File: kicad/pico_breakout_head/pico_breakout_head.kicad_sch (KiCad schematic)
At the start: 16 parts, among them J1 Conn_01x03, J2 JST PH 5-pin male thru vertic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, J3 Conn_01x03, J34 Conn_01x03, J4 Conn_01x03, J5 XH2.54

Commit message: PCB updated to product
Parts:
- removed J2: JST PH 5-pin male thru vertical, Connector_JST:JST_PH_B5B-PH-K_1x05_P2.00mm_Vertical, symbol Connector_Generic:Conn_01x05
- added J2: Conn_01x06, symbol Connector_Generic:Conn_01x06
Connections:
- net +5V: now also U2.39 (VSYS), J2.1 (Pin_1); no longer U2.40 (VBUS)
- net GND: now also J2.6 (Pin_6)
- net SCL_ESP32: now also J2.3 (Pin_3)
- net SDA_ESP32: now also J2.4 (Pin_4)
- new net INT_ESP32: J2.5 (Pin_5)
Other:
- moved on the sheet: U2

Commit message: Pico head WiP
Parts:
- removed J2: Conn_01x06, symbol Connector_Generic:Conn_01x06
- removed J3, J34, J4: Conn_01x03, symbol Connector_Generic:Conn_01x03
- added H1, H2, H3, H4: MountingHole, MountingHole:MountingHole_3.2mm_M3, symbol Mechanical:MountingHole
- added J1: JST B6B-PH-K-S, Connector_JST:JST_PH_B6B-PH-K_1x06_P2.00mm_Vertical, symbol Connector_Generic:Conn_01x06
- added J2, J3: HDR F 2.54MM 20-pin VERT, symbol Connector_Generic:Conn_01x20
- added J4: HDR M 2.54MM 9-pin VERT, symbol Connector_Generic:Conn_01x09
- renumbered J1 to J6
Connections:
- net +3.3V: now also J3.5 (Pin_5)
- net +5V: now also J1.1 (Pin_1), J3.2 (Pin_2), J4.2 (Pin_2), J4.4 (Pin_4), J4.7 (Pin_7)
- net GND: now also J1.6 (Pin_6), J2.13 (Pin_13), J2.18 (Pin_18), J2.8 (Pin_8), J3.13 (Pin_13), J3.18 (Pin_18), J3.3 (Pin_3), J3.8 (Pin_8), J4.1 (Pin_1), J4.5 (Pin_5), J4.8 (Pin_8)
- net SERVO_LEFT: now also U2.5 (I2C1_SCL/SPI0_TX/GP3), J2.5 (Pin_5), J4.3 (Pin_3)
- net SERVO_RIGHT: now also U2.6 (UART1_TX/I2C0_SDA/SPI0_RX/GP4), J2.6 (Pin_6), J4.6 (Pin_6)
- net I2C_SDA_MASTER: now reaches U2.1 (UART0_TX/I2C0_SDA/SPI0_RX/GP0)
- net I2C_SDA_MASTER: now also J1.4 (Pin_4), J2.1 (Pin_1)
- net at U2.10 (I2C1_SCL/SPI0_TX/GP7): now also J2.10 (Pin_10)
- net at U2.11 (UART1_TX/I2C0_SDA/SPI1_RX/GP8): now also J2.11 (Pin_11)
- net at U2.12 (UART1_RX/I2C0_SCL/SPI1_CSn/GP9): now also J2.12 (Pin_12)
- net at U2.14 (I2C1_SDA/SPI1_SCK/GP10): now also J2.14 (Pin_14)
- net at U2.15 (I2C1_SCL/SPI1_TX/GP11): now also J2.15 (Pin_15)
- net at U2.16 (UART0_TX/I2C0_SDA/SPI1_RX/GP12): now also J2.16 (Pin_16)
- net at U2.17 (UART0_RX/I2C0_SCL/SPI1_CSn/GP13): now also J2.17 (Pin_17)
- net at U2.19 (I2C1_SDA/SPI1_SCK/GP14): now also J2.19 (Pin_19)
- net I2C_SCL_MASTER: now reaches U2.2 (UART0_RX/I2C0_SCL/SPI0_CSn/GP1)
- net I2C_SCL_MASTER: now also J1.3 (Pin_3), J2.2 (Pin_2)
- net at U2.20 (I2C1_SCL/SPI1_TX/GP15): now also J2.20 (Pin_20)
- net at U2.21 (GP16/SPI0_RX/I2C0_SDA/UART0_TX): now also J3.20 (Pin_20)
- net at U2.22 (GP17/SPI0_CSn/I2C0_SCL/UART0_RX): now also J3.19 (Pin_19)
- net at U2.24 (GP18/SPI0_SCK/I2C1_SDA): now also J3.17 (Pin_17)
- net at U2.25 (GP19/SPI0_TX/I2C1_SCL): now also J3.16 (Pin_16)
- net at U2.26 (GP20/I2C0_SDA): now also J3.15 (Pin_15)
- net at U2.27 (GP21/I2C0_SCL): now also J3.14 (Pin_14)
- net at U2.29 (GP22): now also J3.12 (Pin_12)
- net at U2.30 (RUN): now also J3.11 (Pin_11)
- net at U2.31 (GP26/ADC0/I2C1_SDA): now also J3.10 (Pin_10)
- net at U2.32 (GP27/ADC1/I2C1_SCL): now also J3.9 (Pin_9)
- net at U2.34 (GP28/ADC2): now also J3.7 (Pin_7)
- net at U2.35 (ADC_VREF): now also J3.6 (Pin_6)
- net at U2.37 (3V3_EN): now also J3.4 (Pin_4)
- net INT_MASTER: now reaches U2.4 (I2C1_SDA/SPI0_SCK/GP2)
- net INT_MASTER: now also J1.5 (Pin_5), J2.4 (Pin_4)
- net at U2.40 (VBUS): now also J3.1 (Pin_1)
- net SERVO_EXT: now reaches U2.7 (UART1_RX/I2C0_SCL/SPI0_CSn/GP5)
- net SERVO_EXT: now also J2.7 (Pin_7), J4.9 (Pin_9)
- net at U2.9 (I2C1_SDA/SPI0_SCK/GP6): now also J2.9 (Pin_9)
- no-connect marks 5 -> 1
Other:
- note added: "I2C MASTER"
- note added: "SERVOS 5V MG90S, SG90S, P0025"
- note removed: "2.54mm header"
- note removed: "TODO - mic array"
- moved on the sheet: J5, U2

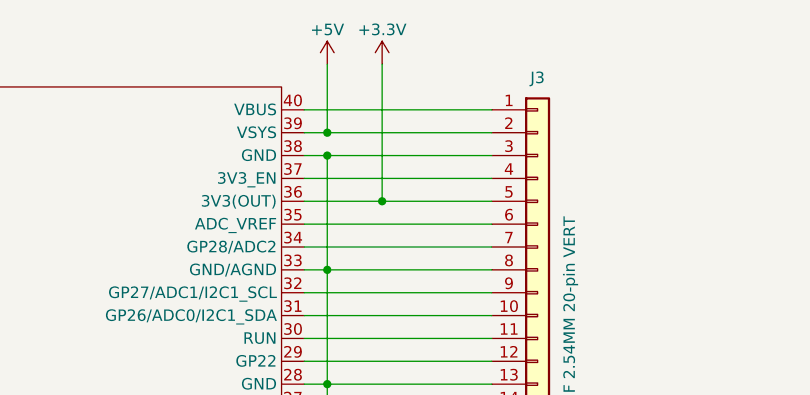
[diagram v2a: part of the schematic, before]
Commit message: 5V OR Schottky diode
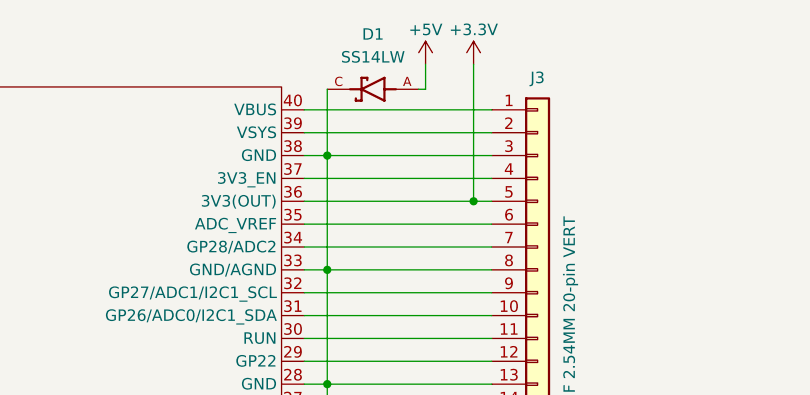
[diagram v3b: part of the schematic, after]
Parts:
- added D1: SS14LW, SS14LW:DIO_SS14LW, symbol Makerspet:SS14LW
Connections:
- net +5V: now also D1.A; no longer J3.2 (Pin_2), U2.39 (VSYS)
- net GND: now also D1.C
- new net: J3.2 (Pin_2), U2.39 (VSYS)
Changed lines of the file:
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@@
   (junction (at 149.098 41.402) (diameter 0) (color 0 0 0 0)
   )
-  (junction (at 155.194 46.482) (diameter 0) (color 0 0 0 0)
-  )
   (junction (at 73.025 161.925) (diameter 0) (color 0 0 0 0)
   )
@@
   (junction (at 67.818 54.102) (diameter 0) (color 0 0 0 0)
   )
-  (junction (at 149.098 38.862) (diameter 0) (color 0 0 0 0)
+  (junction (at 165.354 46.482) (diameter 0) (color 0 0 0 0)
   )
   (junction (at 86.995 136.525) (diameter 0) (color 0 0 0 0)
@@
     (stroke (width 0) (type default))
   )
-  (wire (pts (xy 146.558 38.862) (xy 149.098 38.862))
+  (wire (pts (xy 146.558 38.862) (xy 167.386 38.862))
     (stroke (width 0) (type default))
   )
@@
     (stroke (width 0) (type default))
   )
-  (wire (pts (xy 149.098 31.242) (xy 149.098 38.862))
-    (stroke (width 0) (type default))
-  )
   (wire (pts (xy 149.098 54.102) (xy 167.386 54.102))
     (stroke (width 0) (type default))
@@
     (stroke (width 0) (type default))
   )
+  (wire (pts (xy 160.02 34.036) (xy 160.02 31.242))
+    (stroke (width 0) (type default))
+  )
   (wire (pts (xy 49.53 46.482) (xy 70.358 46.482))
     (stroke (width 0) (type default))
@@
     (stroke (width 0) (type default))
   )
+  (wire (pts (xy 159.258 34.036) (xy 160.02 34.036))
+    (stroke (width 0) (type default))
+  )
   (wire (pts (xy 93.345 136.525) (xy 118.745 136.525))
     (stroke (width 0) (type default))
@@
     (stroke (width 0) (type default))
   )
+  (wire (pts (xy 165.354 46.482) (xy 167.386 46.482))
+    (stroke (width 0) (type default))
+  )
   (wire (pts (xy 146.558 76.962) (xy 167.386 76.962))
     (stroke (width 0) (type default))
   )
-  (wire (pts (xy 155.194 46.482) (xy 167.386 46.482))
-    (stroke (width 0) (type default))
-  )
   (wire (pts (xy 186.944 149.606) (xy 185.674 149.606))
     (stroke (width 0) (type default))
@@
     (stroke (width 0) (type default))
   )
-  (wire (pts (xy 146.558 46.482) (xy 155.194 46.482))
+  (wire (pts (xy 146.558 46.482) (xy 165.354 46.482))
     (stroke (width 0) (type default))
   )
@@
     (stroke (width 0) (type default))
   )
+  (wire (pts (xy 149.098 34.036) (xy 149.098 41.402))
+    (stroke (width 0) (type default))
+  )
   (wire (pts (xy 49.53 82.042) (xy 70.358 82.042))
     (stroke (width 0) (type default))
@@
     (stroke (width 0) (type default))
   )
-  (wire (pts (xy 149.098 38.862) (xy 167.386 38.862))
-    (stroke (width 0) (type default))
-  )
   (wire (pts (xy 71.755 154.305) (xy 73.025 154.305))
     (stroke (width 0) (type default))
@@
     (stroke (width 0) (type default))
   )
-  (wire (pts (xy 155.194 31.242) (xy 155.194 46.482))
+  (wire (pts (xy 165.354 31.242) (xy 165.354 46.482))
     (stroke (width 0) (type default))
   )
@@
     )
   )
-  (symbol (lib_id "power:+5V") (at 149.098 31.242 0) (unit 1)
+  (symbol (lib_id "power:+5V") (at 160.02 31.242 0) (unit 1)
     (in_bom yes) (on_board yes) (dnp no) (fields_autoplaced)
-    (property "Reference" "#PWR05" (at 149.098 35.052 0)
-      (effects (font (size 1.27 1.27)) hide)
-    )
-    (property "Value" "+5V" (at 149.098 27.432 0)
-      (effects (font (size 1.27 1.27)))
-    )
-    (property "Footprint" "" (at 149.098 31.242 0)
-      (effects (font (size 1.27 1.27)) hide)
-    )
-    (property "Datasheet" "" (at 149.098 31.242 0)
+    (property "Reference" "#PWR05" (at 160.02 35.052 0)
+      (effects (font (size 1.27 1.27)) hide)
+    )
+    (property "Value" "+5V" (at 160.02 27.432 0)
+      (effects (font (size 1.27 1.27)))
+    )
+    (property "Footprint" "" (at 160.02 31.242 0)
+      (effects (font (size 1.27 1.27)) hide)
+    )
+    (property "Datasheet" "" (at 160.02 31.242 0)
       (effects (font (size 1.27 1.27)) hide)
     )
@@
     )
   )
-  (symbol (lib_id "power:+3.3V") (at 155.194 31.242 0) (unit 1)
+  (symbol (lib_id "power:+3.3V") (at 165.354 31.242 0) (unit 1)
     (in_bom yes) (on_board yes) (dnp no) (fields_autoplaced)
-    (property "Reference" "#PWR053" (at 155.194 35.052 0)
-      (effects (font (size 1.27 1.27)) hide)
-    )
-    (property "Value" "+3.3V" (at 155.194 27.432 0)
-      (effects (font (size 1.27 1.27)))
-    )
-    (property "Footprint" "" (at 155.194 31.242 0)
-      (effects (font (size 1.27 1.27)) hide)
-    )
-    (property "Datasheet" "" (at 155.194 31.242 0)
+    (property "Reference" "#PWR053" (at 165.354 35.052 0)
+      (effects (font (size 1.27 1.27)) hide)
+    )
+    (property "Value" "+3.3V" (at 165.354 27.432 0)
+      (effects (font (size 1.27 1.27)))
+    )
+    (property "Footprint" "" (at 165.354 31.242 0)
+      (effects (font (size 1.27 1.27)) hide)
+    )
+    (property "Datasheet" "" (at 165.354 31.242 0)
       (effects (font (size 1.27 1.27)) hide)
     )
@@
         )
       )
+    )
+  )
+  (symbol (lib_id "Makerspet:SS14LW") (at 154.178 34.036 180) (unit 1)
+    (in_bom yes) (on_board yes) (dnp no) (fields_autoplaced)
+    (property "Reference" "D1" (at 154.178 27.94 0)
+      (effects (font (size 1.27 1.27)))
+    )
+    (property "Value" "SS14LW" (at 154.178 30.48 0)
+      (effects (font (size 1.27 1.27)))
+    )
+    (property "Footprint" "SS14LW:DIO_SS14LW" (at 154.178 27.686 0)
+      (effects (font (size 1.27 1.27)) (justify bottom) hide)
+    )
+    (property "Datasheet" "" (at 154.178 34.036 0)
+      (effects (font (size 1.27 1.27)) hide)
+    )
+    (pin "C")
+    (pin "A")
+    (instances
+      (project "pico_breakout_head"
+        (path "/e24ae185-8f18-408c-aee8-f727519bade3"
+          (reference "D1") (unit 1)
+        )
+      )

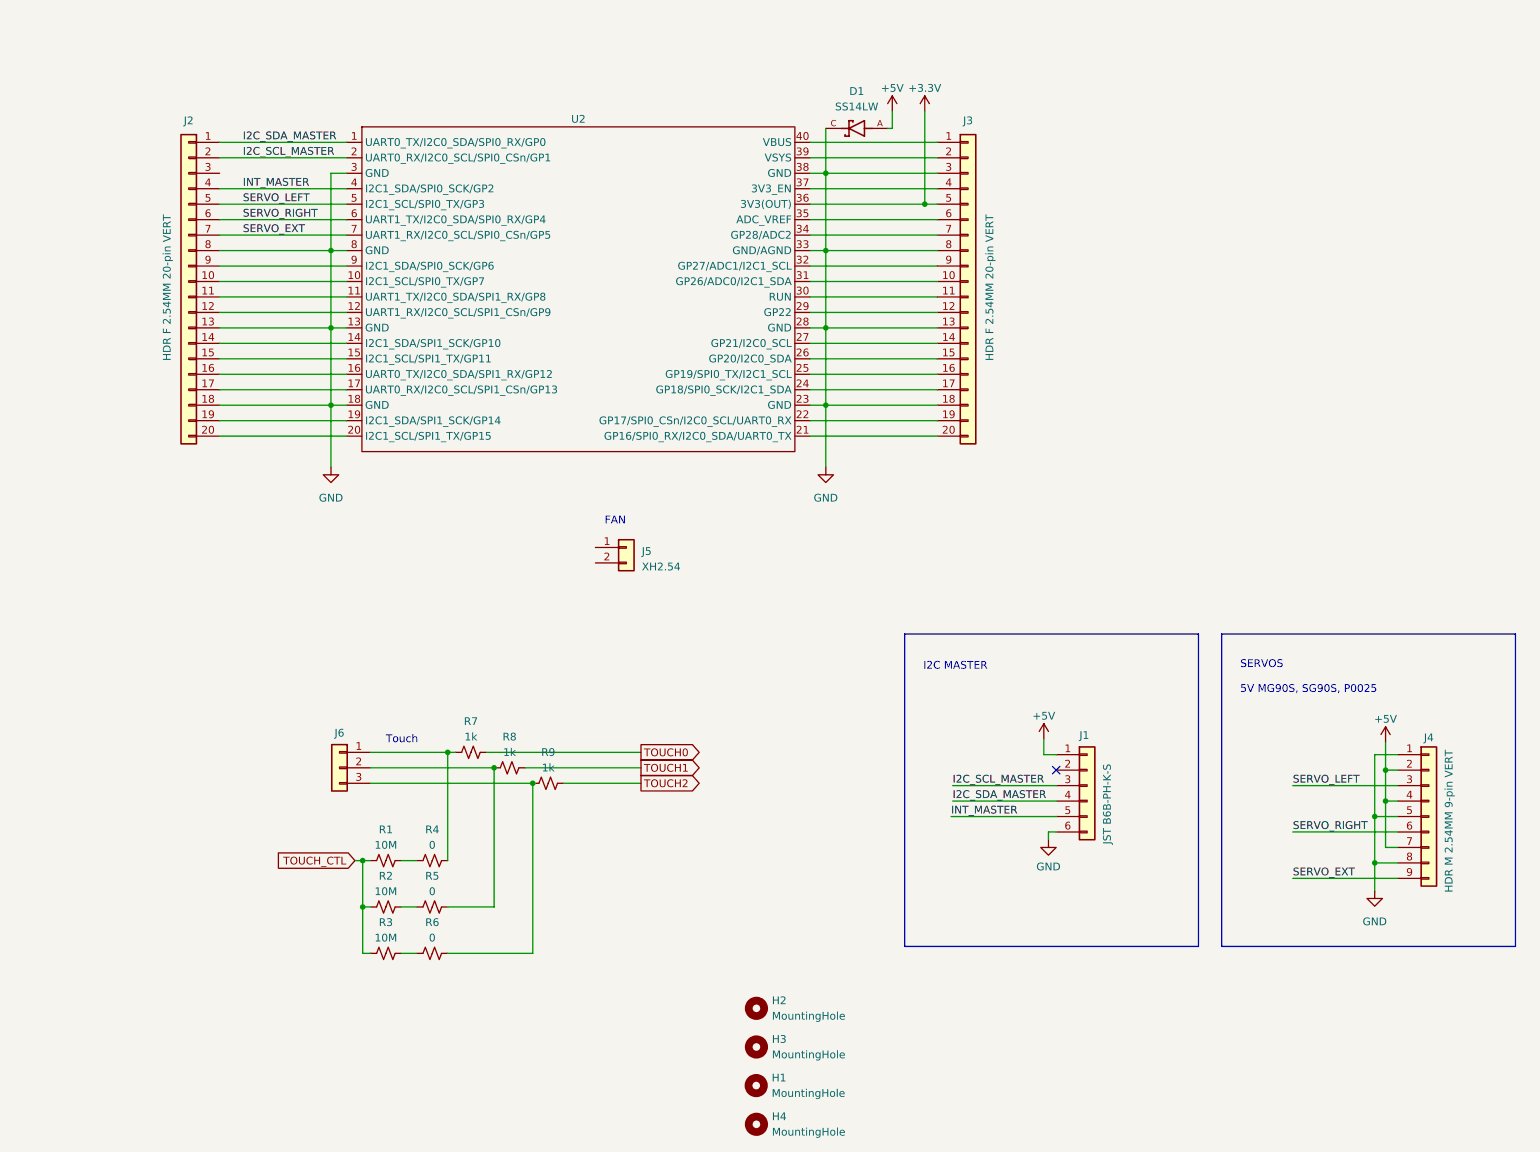
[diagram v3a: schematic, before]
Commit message: Pico head breakout layout start
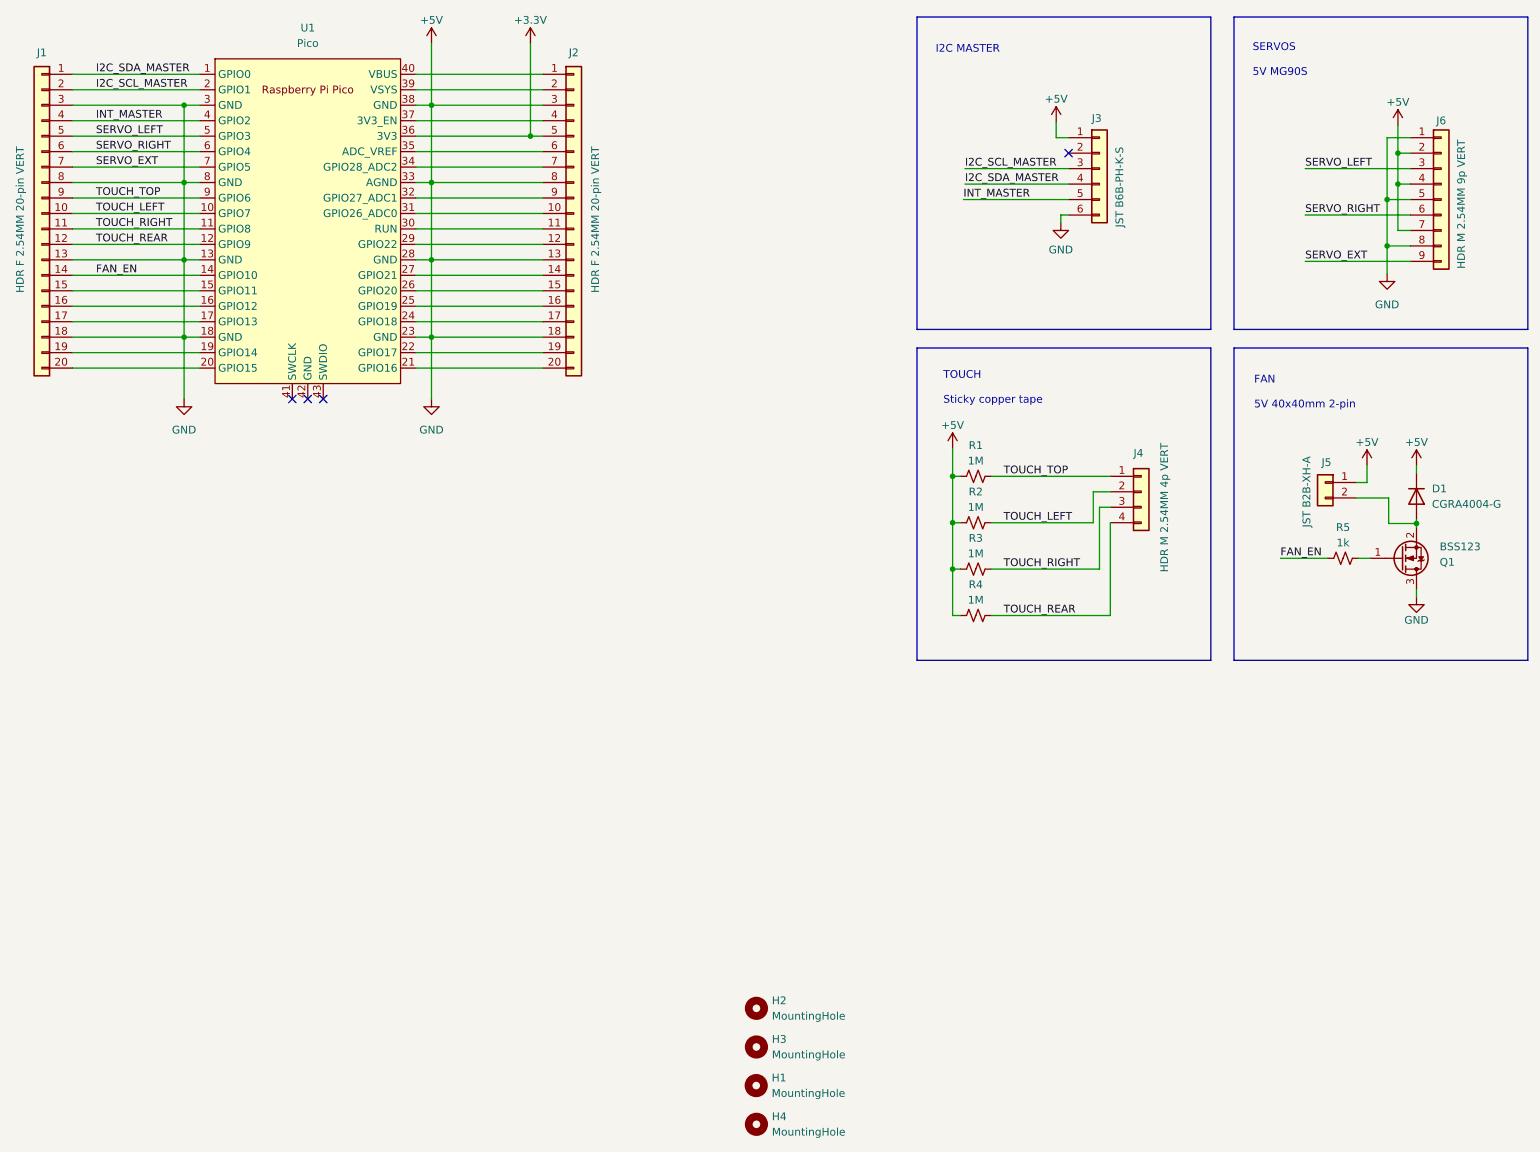
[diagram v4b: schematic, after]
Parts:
- removed D1: SS14LW, SS14LW:DIO_SS14LW, symbol Makerspet:SS14LW
- removed J3: HDR F 2.54MM 20-pin VERT, symbol Connector_Generic:Conn_01x20
- removed J6: Conn_01x03, symbol Connector_Generic:Conn_01x03
- removed R6: 0, symbol Device:R_Small_US
- removed R7, R8, R9: 1k, symbol Device:R_Small_US
- removed U2: ~, symbol Kaia_v2:RASPBERRY-PI-PICO
- added D1: CGRA4004-G, Diode_SMD:D_SMA, symbol Device:D
- added J2: HDR F 2.54MM 20-pin VERT, Connector_PinHeader_2.54mm:PinHeader_1x20_P2.54mm_Vertical, symbol Connector_Generic:Conn_01x20
- added J4: HDR M 2.54MM 4p VERT, Connector_PinHeader_2.54mm:PinHeader_1x04_P2.54mm_Vertical, symbol Connector_Generic:Conn_01x04
- added Q1: BSS123, Package_TO_SOT_SMD:SOT-23, symbol Transistor_FET:BSS123
- added U1: Pico, Makerspet:RPi_Pico_SMD_TH, symbol Makerspet:Pico
- J1: renamed from J2; footprint (none) -> Connector_PinHeader_2.54mm:PinHeader_1x20_P2.54mm_Vertical
- J5: value XH2.54 -> JST B2B-XH-A
- J6: renamed from J4; value HDR M 2.54MM 9-pin VERT -> HDR M 2.54MM 9p VERT; footprint (none) -> Connector_PinHeader_2.54mm:PinHeader_1x09_P2.54mm_Vertical
- R1, R2, R3: value 10M -> 1M; footprint (none) -> Resistor_SMD:R_0603_1608Metric
- R4: value 0 -> 1M; footprint (none) -> Resistor_SMD:R_0603_1608Metric
- R5: value 0 -> 1k; footprint (none) -> Resistor_SMD:R_0603_1608Metric
- renumbered J1 to J3
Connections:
- net GND is gone; now on net +5V: J1.13 (Pin_13), J1.18 (Pin_18), J1.8 (Pin_8), J3.6 (Pin_6), J6.1 (Pin_1), J6.5 (Pin_5), J6.8 (Pin_8)
- net TOUCH_CTL is gone; now on net +5V: R1.2, R2.2, R3.2
- net +3.3V: now also J2.5 (Pin_5), U1.36 (3V3)
- net +5V: now also J1.3 (Pin_3), J5.1 (Pin_1), R4.2, D1.1 (K), J2.13 (Pin_13), J2.18 (Pin_18), J2.3 (Pin_3), J2.8 (Pin_8), Q1.3 (D), U1.13 (GND), U1.18 (GND), U1.23 (GND), U1.28 (GND), U1.3 (GND), U1.33 (AGND), U1.38 (GND), U1.8 (GND)
- net I2C_SCL_MASTER: now also U1.2 (GPIO1)
- net I2C_SDA_MASTER: now also U1.1 (GPIO0)
- net INT_MASTER: now also U1.4 (GPIO2)
- net SERVO_EXT: now also U1.7 (GPIO5)
- net SERVO_LEFT: now also U1.5 (GPIO3)
- net SERVO_RIGHT: now also U1.6 (GPIO4)
- net TOUCH_RIGHT: now reaches R3.1
- net TOUCH_RIGHT: now also J1.11 (Pin_11), J4.3 (Pin_3), U1.11 (GPIO8)
- net FAN_EN: now reaches R5.2
- net FAN_EN: now also J1.14 (Pin_14), U1.14 (GPIO10); no longer R2.1
- net at J5.2 (Pin_2): now also D1.2 (A), Q1.2 (S)
- net at R5.1: now also Q1.1 (G)
- net TOUCH_REAR: now reaches R4.1
- net TOUCH_REAR: now also J1.12 (Pin_12), J4.4 (Pin_4), U1.12 (GPIO9)
- net TOUCH_TOP: now reaches R1.1
- net TOUCH_TOP: now also J1.9 (Pin_9), J4.1 (Pin_1), U1.9 (GPIO6); no longer R4.2
- net TOUCH_LEFT: now reaches J1.10 (Pin_10)
- net TOUCH_LEFT: now also R2.1, J4.2 (Pin_2), U1.10 (GPIO7)
- net at J1.15 (Pin_15): now also U1.15 (GPIO11)
- net at J1.16 (Pin_16): now also U1.16 (GPIO12)
- net at J1.17 (Pin_17): now also U1.17 (GPIO13)
- net at J1.19 (Pin_19): now also U1.19 (GPIO14)
- net at J1.20 (Pin_20): now also U1.20 (GPIO15)
- new net: J2.1 (Pin_1), U1.40 (VBUS)
- new net: J2.10 (Pin_10), U1.31 (GPIO26_ADC0)
- new net: J2.11 (Pin_11), U1.30 (RUN)
- new net: J2.12 (Pin_12), U1.29 (GPIO22)
- new net: J2.14 (Pin_14), U1.27 (GPIO21)
- new net: J2.15 (Pin_15), U1.26 (GPIO20)
- new net: J2.16 (Pin_16), U1.25 (GPIO19)
- new net: J2.17 (Pin_17), U1.24 (GPIO18)
- new net: J2.19 (Pin_19), U1.22 (GPIO17)
- new net: J2.2 (Pin_2), U1.39 (VSYS)
- new net: J2.20 (Pin_20), U1.21 (GPIO16)
- new net: J2.4 (Pin_4), U1.37 (3V3_EN)
- new net: J2.6 (Pin_6), U1.35 (ADC_VREF)
- new net: J2.7 (Pin_7), U1.34 (GPIO28_ADC2)
- new net: J2.9 (Pin_9), U1.32 (GPIO27_ADC1)
- no-connect marks 1 -> 4
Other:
- note added: "FAN 5V 40x40mm 2-pin"
- note added: "SERVOS 5V MG90S"
- note added: "TOUCH Sticky copper tape"
- note removed: "FAN"
- note removed: "SERVOS 5V MG90S, SG90S, P0025"
- note removed: "Touch"
- moved on the sheet: J1, J3, J6, R1, R2, R3
